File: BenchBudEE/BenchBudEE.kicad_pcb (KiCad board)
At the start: 4 copper layers, 165.1 x 63.5 mm, 73 parts, among them K1 1461069-5, P1 24Pin MiniFit JR, P2 CONN_3X2, P3 CONN_2, P4 12 Pin Terminal Block, P5 3 Pin TB, Q1 2N3904, Q2 DMN65D8L-7, Q3 MOS_N_NUM, Q4 MOS_N_NUM, U1 LTV-816S, U3 MCP4801, U4 OPA4170, U5 MCP3901, U6 LMT84

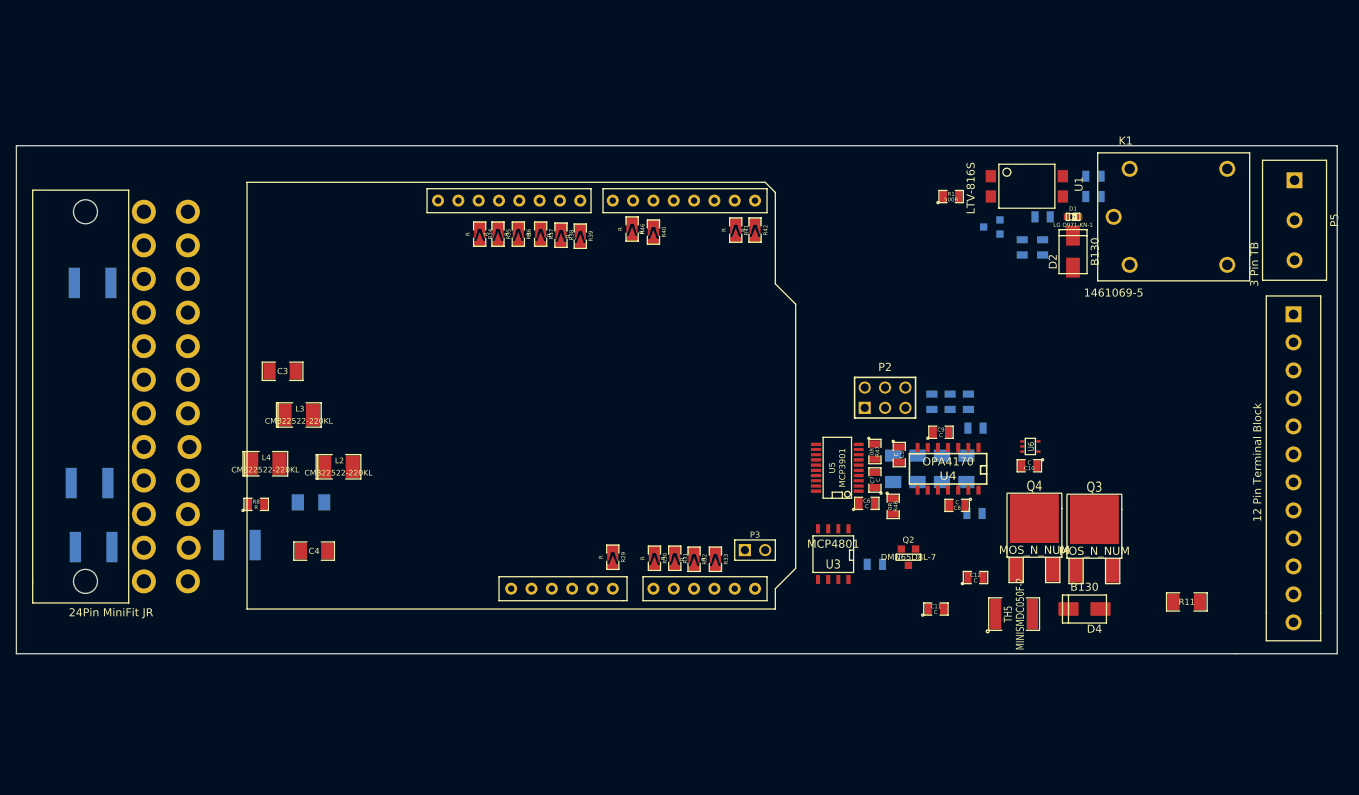
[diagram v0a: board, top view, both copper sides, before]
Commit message: All modules (inc. LED Driver) associated + roughly placed.
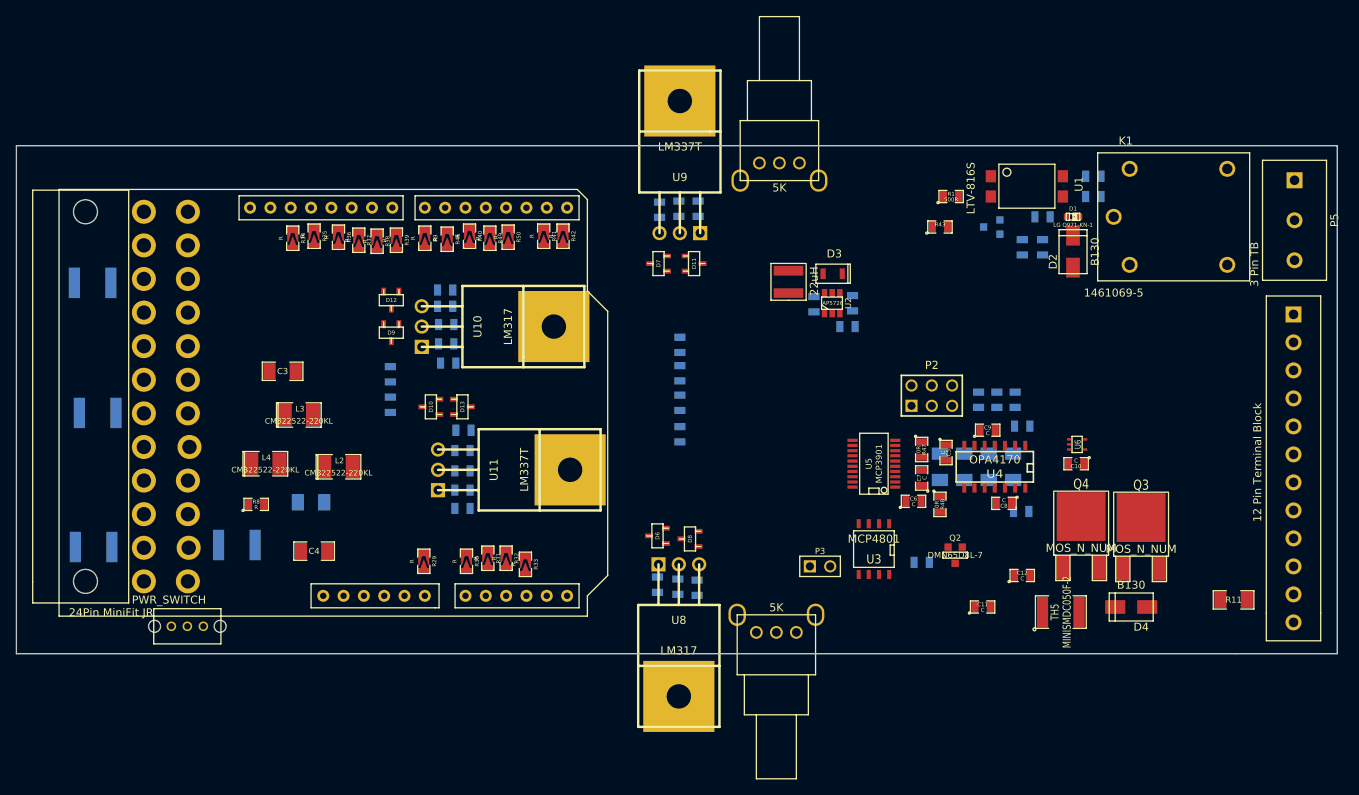
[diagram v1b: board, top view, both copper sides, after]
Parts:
- added C1: 1uF, SM0805, B.Cu at (148.0, 88.4)
- added C14: C, SM0805, B.Cu at (128.4, 123.4)
- added C15: C, SM0805, B.Cu at (128.7, 76.6)
- added C16: C, SM0805, B.Cu at (95.0, 97.2)
- added C17: C, SM0805, B.Cu at (133.3, 123.8)
- added C18: C, SM0805, B.Cu at (95.0, 101.0)
- added C19: C, SM0805, B.Cu at (133.5, 76.5)
- added C2: 1uF, SM0805, B.Cu at (152.8, 88.3)
- added C20: C, SM0805, B.Cu at (104.0, 111.6)
- added C21: C, SM0805, B.Cu at (101.9, 88.6)
- added C22: C, SM0805, B.Cu at (102.0, 93.3)
- added C23: C, SM0805, B.Cu at (104.0, 109.2)
- added C24: C, SM0805, B.Cu at (102.0, 90.9)
- added C25: C, SM0805, B.Cu at (104.0, 106.7)
- added D10: MMBD914-7-F, sot23, F.Cu at (100.1, 101.2)
- added D11: MMBD914-7-F, sot23, F.Cu at (133.0, 83.3)
- added D12: MMBD914-7-F, sot23, F.Cu at (95.1, 87.9)
- added D13: MMBD914-7-F, sot23, F.Cu at (104.0, 101.2)
- added D3: B0540WS-7, SOD323, F.Cu at (149.1, 84.6)
- added D6: MMBD914-7-F, sot23, F.Cu at (128.4, 117.3)
- added D7: MMBD914-7-F, sot23, F.Cu at (128.5, 83.3)
- added D8: MMBD914-7-F, sot23, F.Cu at (132.5, 117.7)
- added D9: MMBD914-7-F, sot23, F.Cu at (95.1, 91.9)
- added L1: 22uH, NR4012, F.Cu at (144.8, 87.0)
- added R19: 5K, POT_5K, F.Cu at (143.3, 129.4)
- added R20: 715R, SM0805, B.Cu at (130.9, 123.7)
- added R21: 715R, SM0805, B.Cu at (131.1, 76.5)
- added R22: 5K, POT_5K, F.Cu at (143.6, 70.7)
- added R23: R, SM0805, B.Cu at (104.0, 113.9)
- added R24: R, SM0805, B.Cu at (104.1, 104.1)
- added R25: R, SM0805, B.Cu at (131.2, 104.6)
- added R26: R, SM0805, B.Cu at (131.2, 100.7)
- added R27: R, SM0805, B.Cu at (131.2, 97.0)
- added R28: R, SM0805, B.Cu at (131.2, 93.5)
- added R43: R, SM0805, F.Cu at (163.7, 78.7)
- added R49: R, SM0805_SolderBridge, F.Cu at (107.4, 80.1)
- added R50: R, SM0805_SolderBridge, F.Cu at (109.7, 80.0)
- added R51: R, SM0805, B.Cu at (101.9, 86.6)
- added R52: R, SM0805, B.Cu at (102.2, 95.8)
- added R7: 15R, SM0805, B.Cu at (152.1, 91.2)
- added R9: R, SM0805_SolderBridge, F.Cu at (99.3, 80.1)
- added SW1: PWR_SWITCH, PWR_SWITCH, F.Cu at (71.6, 128.7)
- added U10: LM317, TO220, F.Cu at (98.9, 91.2)
- added U11: LM337T, TO220, F.Cu at (101.0, 109.1)
- added U2: AP5726, SOT23_6, F.Cu at (150.2, 88.3)
- added U8: LM317, TO220, F.Cu at (131.1, 120.9)
- added U9: LM337T, TO220, F.Cu at (131.2, 79.5)
- moved R42 24.0 mm to (116.6, 79.9)
- moved R41 24.0 mm to (114.2, 79.9)
- moved R33 23.8 mm to (111.9, 120.9)
- moved R29 23.6 mm to (99.2, 120.5)
- moved ARD1 23.5 mm to (117.1, 124.8)
- moved R30 23.5 mm to (104.5, 120.5)
- moved R32 23.5 mm to (109.5, 120.1)
- moved R34 23.4 mm to (82.8, 80.1)
- moved R31 23.4 mm to (107.2, 120.1)
- moved R46 23.1 mm to (102.1, 80.3)
- moved R38 23.0 mm to (93.3, 80.5)
- moved R39 23.0 mm to (95.8, 80.4)
- moved R40 23.0 mm to (104.9, 79.9)
- moved R35 23.0 mm to (85.5, 79.9)
- moved R37 22.7 mm to (91.1, 80.4)
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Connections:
- net N-00000105 renamed /Power/ATX_-12V
- net N-00000118 renamed /Power/ATX_+3V3
- net N-00000126 renamed /Power/ATX_+5V
- P4 pad 5: (no net) -> /PowerAdjustmentMonitor/V-_ADJ
